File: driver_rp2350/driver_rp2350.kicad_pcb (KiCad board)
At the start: 6 copper layers, 45 x 45 mm, 463 parts, among them J1 Conn_01x04, J2 Conn_01x05, J3 Conn_01x05, J4 Conn_01x05, J5 Conn_01x05, SW1 SW_Push, SW2 SW_Push, U1 APS6404L-3SQR, U10 UCC27517, U11 UCC27517, U12 UCC27517, U13 UCC27517, U14 UCC27517, U15 UCC27517, U16 UCC27517, U17 UCC27517, U18 UCC27517, U19 UCC27517, U2 RP2354B_80QFN, U20 UCC27517, U21 UCC27517, U22 UCC27517, U23 UCC27517, U24 UCC27517, U25 UCC27517, U26 UCC27517, U27 UCC27517, U28 UCC27517, U29 UCC27517, U3 UCC27517, U30 UCC27517, U31 UCC27517, U32 UCC27517, U33 UCC27517, U34 UCC27517, U35 UCC27517, U36 UCC27517, U37 UCC27517, U38 UCC27517, U39 AP2112K-3.3, U4 UCC27517, U5 UCC27517, U6 UCC27517, U7 UCC27517, U8 UCC27517, U9 UCC27517, Y1 ABM8-272-T3

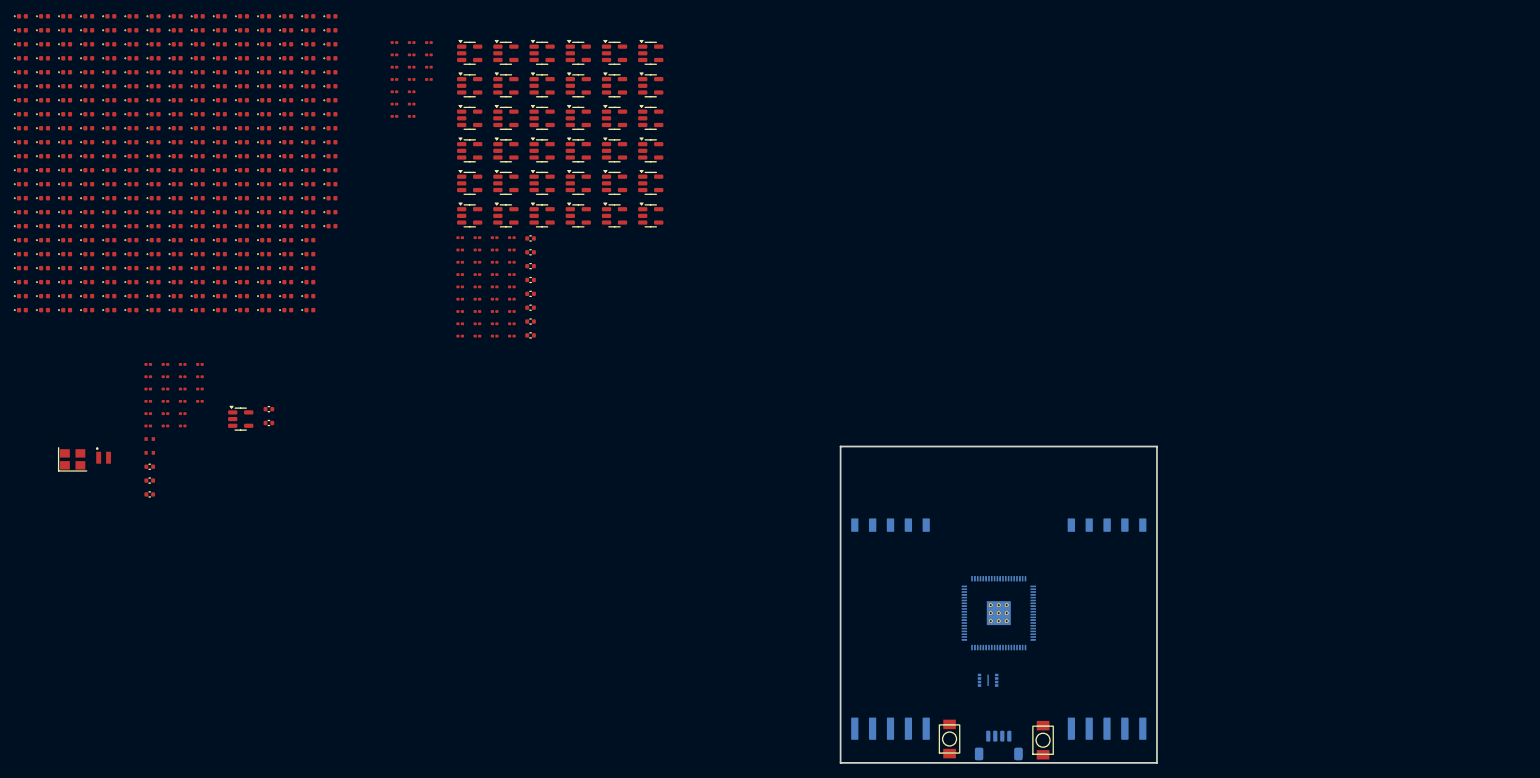
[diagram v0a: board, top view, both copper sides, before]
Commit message: Worked on layout for 18x18 rp2354b panels.
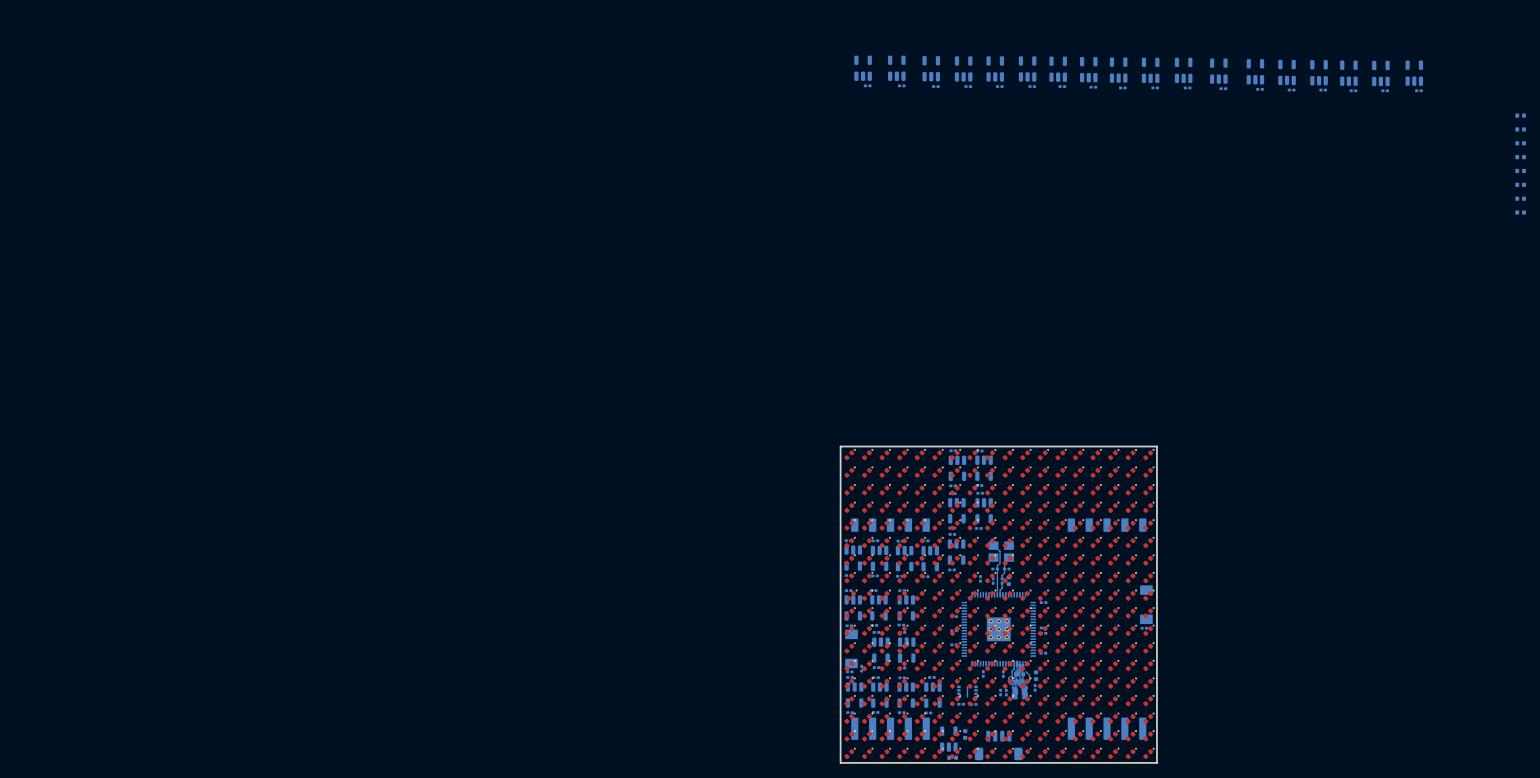
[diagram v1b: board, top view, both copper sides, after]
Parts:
- removed the C19 at (-48.3, 56.8)
- C1, C10, C11, C12, C13, C14, C15, C16, C17, C18, C2, C3, C4, C5, C6, C64, C65, C7, C8, C9, L1, R1, R10, R11, R12, R13, R14, R15, R16, R17, R18, R19, R2, R20, R21, R22, R23, R24, R25, R26, R3, R4, R5, R6, R7, R8, R9, SW1, SW2, U10, U11, U12, U13, U14, U15, U16, U17, U18, U19, U20, U21, U22, U23, U24, U25, U26, U27, U28, U29, U3, U30, U31, U32, U33, U34, U35, U36, U37, U38, U39, U4, U5, U6, U7, U8, U9, Y1: moved to B.Cu
- C19: renamed from C20; moved to B.Cu
- C20: renamed from C21; moved to B.Cu
- C21: renamed from C22; moved to B.Cu
- C22: renamed from C23; moved to B.Cu
- C23: renamed from C24; moved to B.Cu
- C24: renamed from C25; moved to B.Cu
- C25: renamed from C26; moved to B.Cu
- C26: renamed from C27; moved to B.Cu
- C27: renamed from C28; moved to B.Cu
- C28: renamed from C29; moved to B.Cu
- C29: renamed from C30; moved to B.Cu
- C30: renamed from C31; moved to B.Cu
- C31: renamed from C32; moved to B.Cu
- C32: renamed from C33; moved to B.Cu
- C33: renamed from C34; moved to B.Cu
- C34: renamed from C35; moved to B.Cu
- C35: renamed from C36; moved to B.Cu
- C36: renamed from C37; moved to B.Cu
- C37: renamed from C38; moved to B.Cu
- C38: renamed from C39; moved to B.Cu
- C39: renamed from C40; moved to B.Cu
- C40: renamed from C41; moved to B.Cu
- C41: renamed from C42; moved to B.Cu
- C42: renamed from C43; moved to B.Cu
- C43: renamed from C44; moved to B.Cu
- C44: renamed from C45; moved to B.Cu
- C45: renamed from C46; moved to B.Cu
- C46: renamed from C47; moved to B.Cu
- C47: renamed from C48; moved to B.Cu
- C48: renamed from C49; moved to B.Cu
- C49: renamed from C50; moved to B.Cu
- C50: renamed from C51; moved to B.Cu
- C51: renamed from C52; moved to B.Cu
- C52: renamed from C53; moved to B.Cu
- C53: renamed from C54; moved to B.Cu
- C54: renamed from C55; moved to B.Cu
- C55: renamed from C56; moved to B.Cu
- C56: renamed from C57; moved to B.Cu
- C57: renamed from C58; moved to B.Cu
- C58: renamed from C59; moved to B.Cu
- C59: renamed from C60; moved to B.Cu
- C60: renamed from C61; moved to B.Cu
- C61: renamed from C62; moved to B.Cu
- C62: renamed from C63; moved to B.Cu
- moved D69 177.3 mm to (93.8, 86.2), turned to -135 degrees
- moved D52 176.2 mm to (93.8, 88.8), turned to -135 degrees
- moved D35 175.5 mm to (93.8, 91.2), turned to -135 degrees
- moved D18 175.2 mm to (93.8, 93.8), turned to -135 degrees
- moved D68 174.9 mm to (91.2, 83.8), turned to -135 degrees
- moved D51 173.8 mm to (91.2, 86.2), turned to -135 degrees
- moved D34 173.1 mm to (91.2, 88.8), turned to -135 degrees
- moved D17 172.7 mm to (91.2, 91.2), turned to -135 degrees
- moved D67 172.5 mm to (88.8, 81.2), turned to -135 degrees
- moved D50 171.4 mm to (88.8, 83.8), turned to -135 degrees
- moved D33 170.6 mm to (88.8, 86.2), turned to -135 degrees
- moved D16 170.2 mm to (88.8, 88.8), turned to -135 degrees
- moved D49 169.0 mm to (86.2, 81.2), turned to -135 degrees
- moved D32 168.2 mm to (86.2, 83.8), turned to -135 degrees
- moved D15 167.7 mm to (86.2, 86.2), turned to -135 degrees
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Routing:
- net /panel_mcu/XIN: track 0.00 -> 7.76 mm
- net +1V1: track 0.00 -> 4.74 mm
- net /panel_mcu/VREG_LX: track 0.00 -> 4.54 mm
- net Net-(C2-Pad1): track 0.00 -> 3.41 mm
- net /panel_mcu/XOUT: track 0.00 -> 1.77 mm
- net GND: track 0.00 -> 1.55 mm
- net +3V3: track 0.00 -> 1.55 mm
- added copper zone on B.Cu, net (none)
- added copper zone on B.Cu, net +1V1
- added copper zone on B.Cu, net +3V3
- added copper zone on B.Cu, net GND

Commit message: Worked on rp2354 panel layout.
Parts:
- moved C56 111.9 mm to (61.8, 77.8), turned to -90 degrees
- moved U38 108.6 mm to (78.9, 91.8), turned to -90 degrees
- moved C57 108.1 mm to (58.6, 69.5)
- moved C58 105.7 mm to (61.8, 71.8), turned to -90 degrees
- moved C54 104.9 mm to (78.2, 89.3), turned to 0 degrees
- moved U37 97.9 mm to (85.6, 85.7), turned to -90 degrees
- moved U36 94.7 mm to (89.4, 85.7), turned to -90 degrees
- moved C53 94.0 mm to (85.0, 83.2), turned to 0 degrees
- moved C62 93.0 mm to (83.2, 84.6), turned to -90 degrees
- moved U35 92.3 mm to (93.0, 85.7), turned to -90 degrees
- moved C52 90.5 mm to (88.8, 83.2), turned to 0 degrees
- moved C61 88.6 mm to (68.4, 56.2), turned to -90 degrees
- moved C60 88.1 mm to (83.2, 73.8), turned to -90 degrees
- moved C51 87.9 mm to (92.5, 83.2), turned to 0 degrees
- moved C55 86.8 mm to (77.9, 55.8)
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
